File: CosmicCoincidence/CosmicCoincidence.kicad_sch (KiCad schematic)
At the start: 14 parts, among them J1 SJ-43515RS-SMT-TR, J2 SJ-43515RS-SMT-TR, J3 SJ-43515RS-SMT-TR, J4 SJ-43515RS-SMT-TR, J5 SJ-43515RS-SMT-TR, J6 SJ-43515RS-SMT-TR, J7 SJ-43515RS-SMT-TR, J8 SJ-43515RS-SMT-TR, J9 USB_C_Receptacle_USB2.0_14P, SW1 Reset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

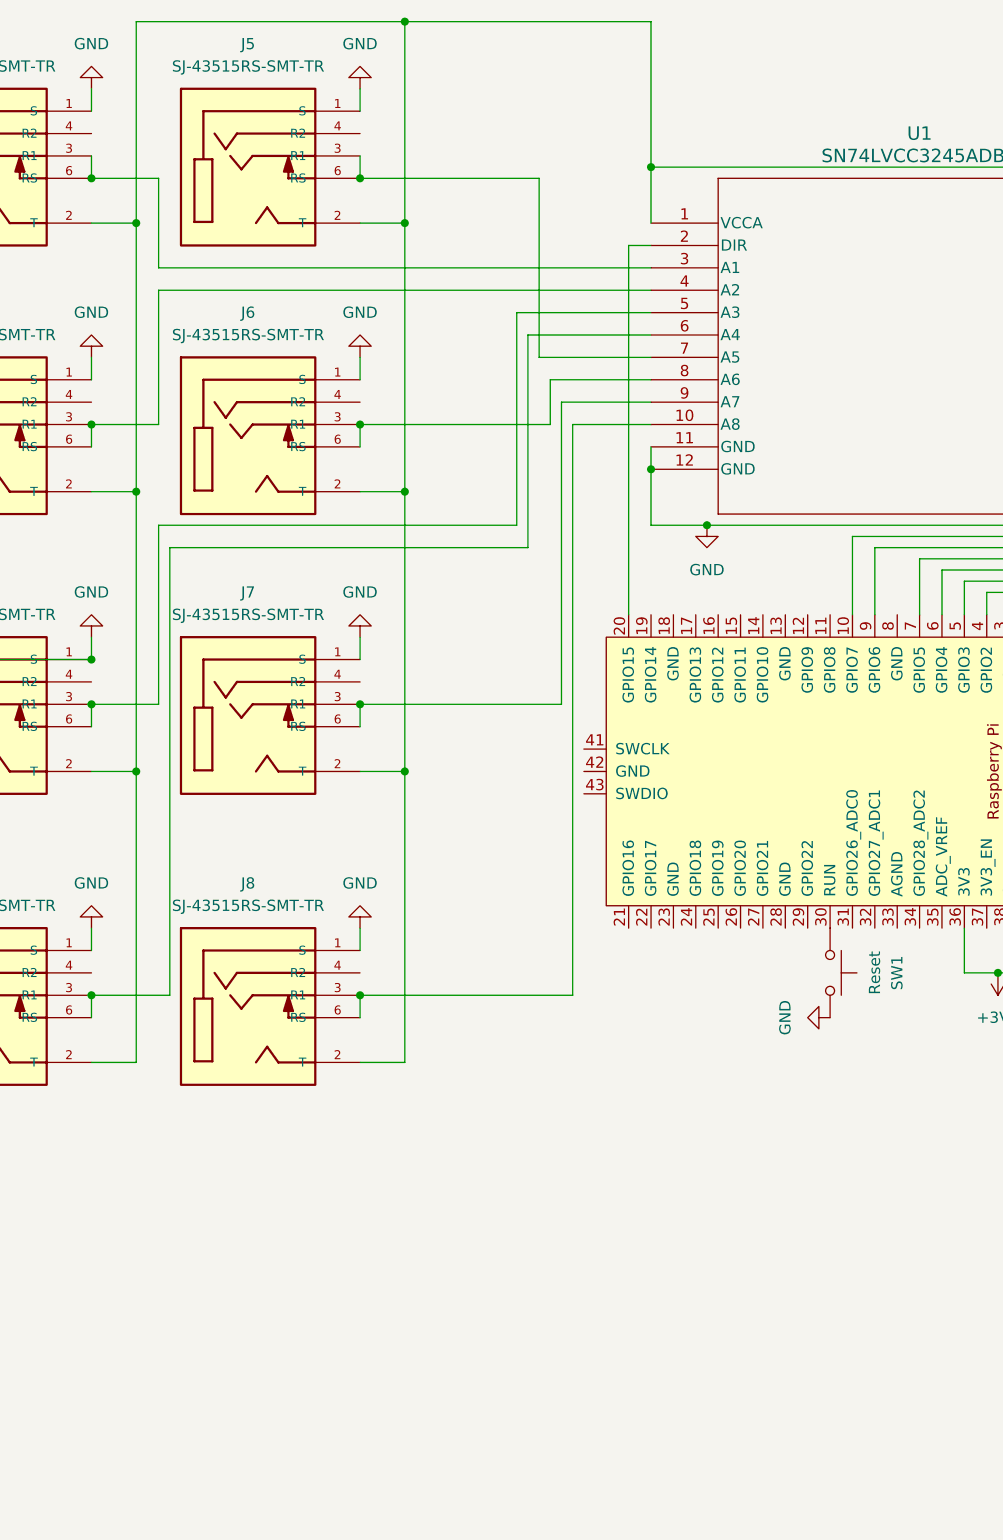
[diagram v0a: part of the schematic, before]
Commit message: Pulldowns on Data Lines
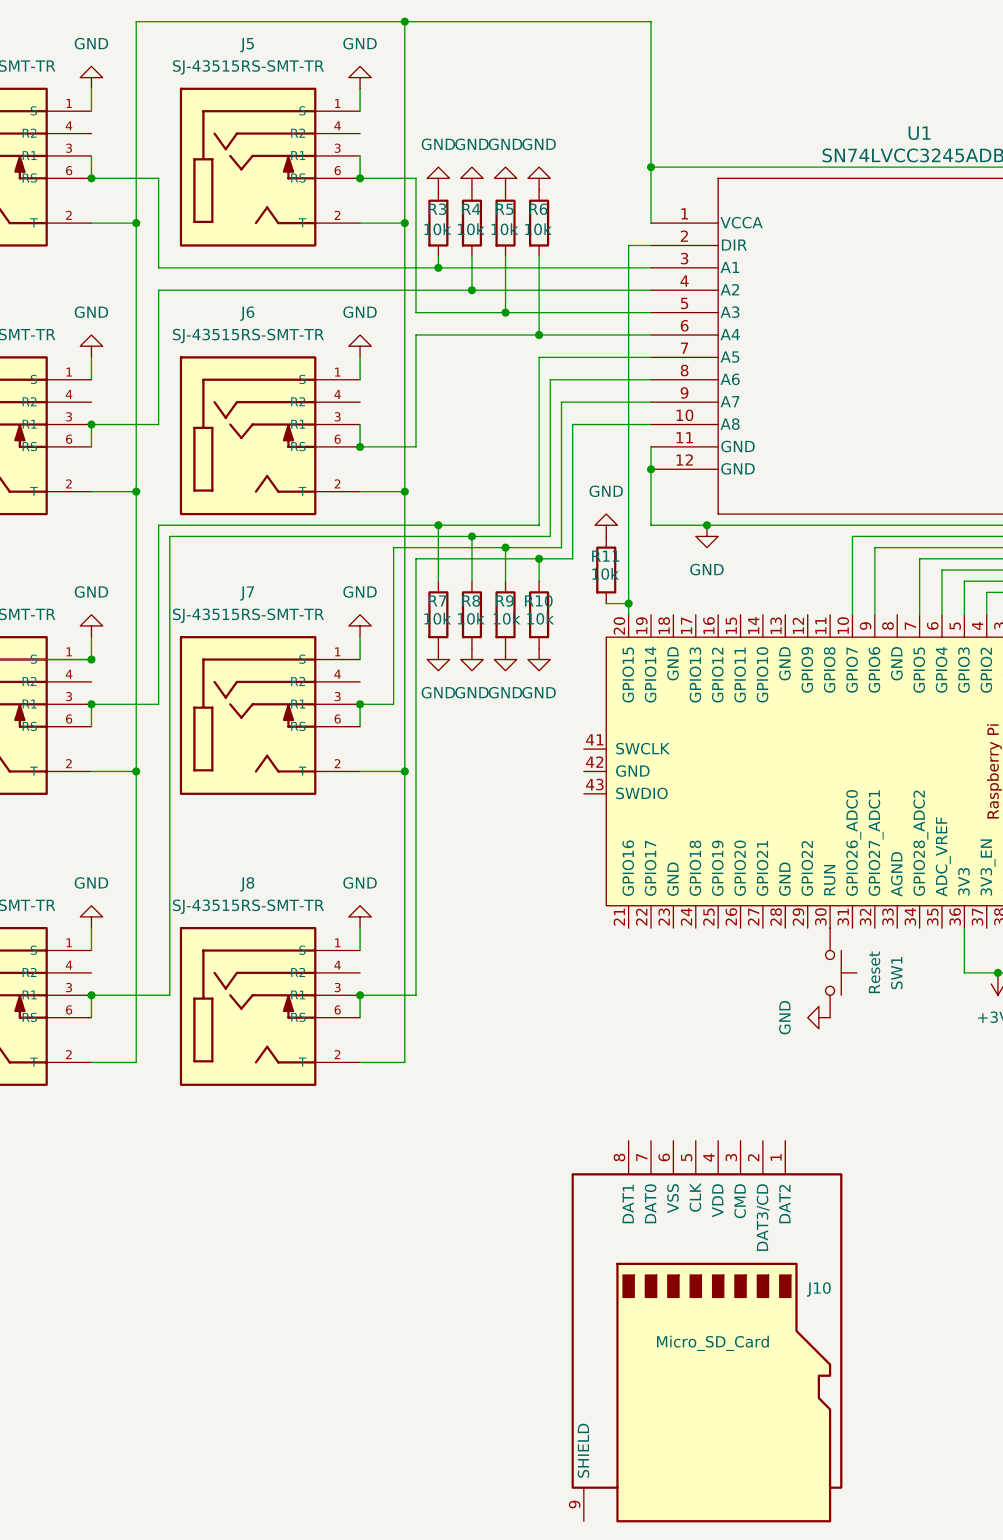
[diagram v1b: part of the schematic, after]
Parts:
- added J10: Micro_SD_Card, symbol Connector:Micro_SD_Card
- added R10, R11, R3, R4, R5, R6, R7, R8, R9: 10k, symbol Device:R
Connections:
- net GND: now also R10.2, R11.1, R3.1, R4.1, R5.1, R6.1, R7.2, R8.2, R9.2
- net at J6.3 (R1), J6.6 (RS): now also U1.6 (A4), R6.2; no longer U1.8 (A6)
- net at J8.3 (R1), J8.6 (RS), U1.10 (A8): now also R10.1
- net at U1.2 (DIR), U2.20 (GPIO15): now also R11.2
- net at J1.3 (R1), J1.6 (RS), U1.3 (A1): now also R3.2
- net at J2.3 (R1), J2.6 (RS), U1.4 (A2): now also R4.2
- net at J3.3 (R1), J3.6 (RS): now also U1.7 (A5), R7.1; no longer U1.5 (A3)
- net at J4.3 (R1), J4.6 (RS): now also U1.8 (A6), R8.1; no longer U1.6 (A4)
- net at J5.3 (R1), J5.6 (RS): now also U1.5 (A3), R5.2; no longer U1.7 (A5)
- net at J7.3 (R1), J7.6 (RS), U1.9 (A7): now also R9.1

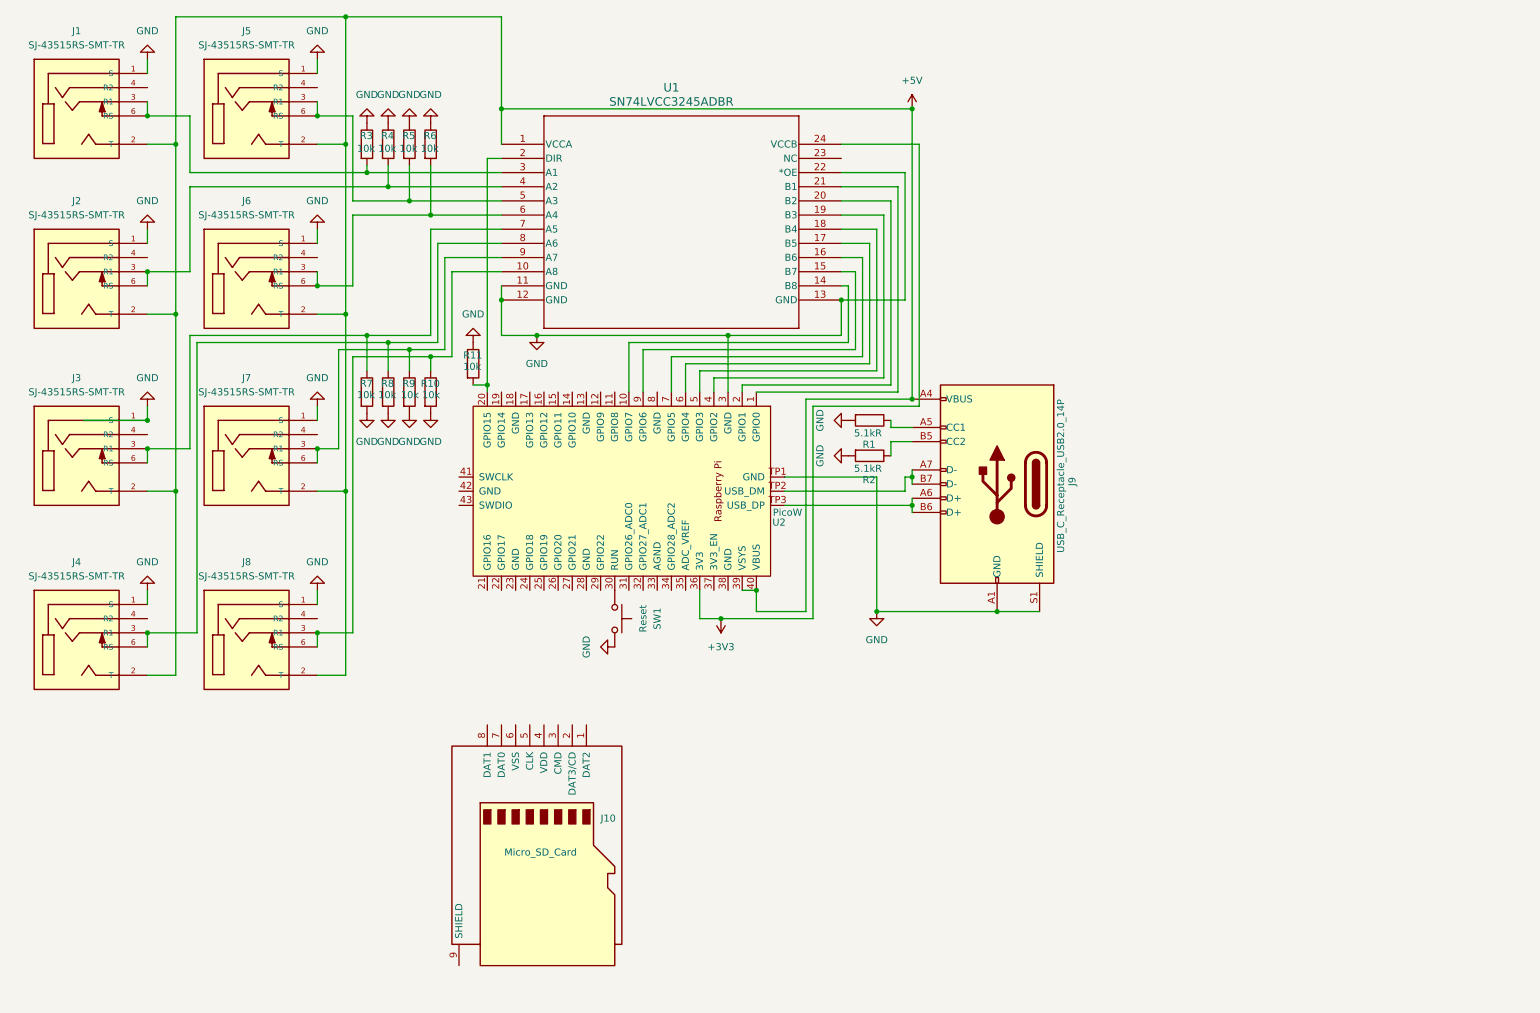
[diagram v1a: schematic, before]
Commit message: Prototype 2
Addition of Power Control, Microsd card, and OLED I2C Screen
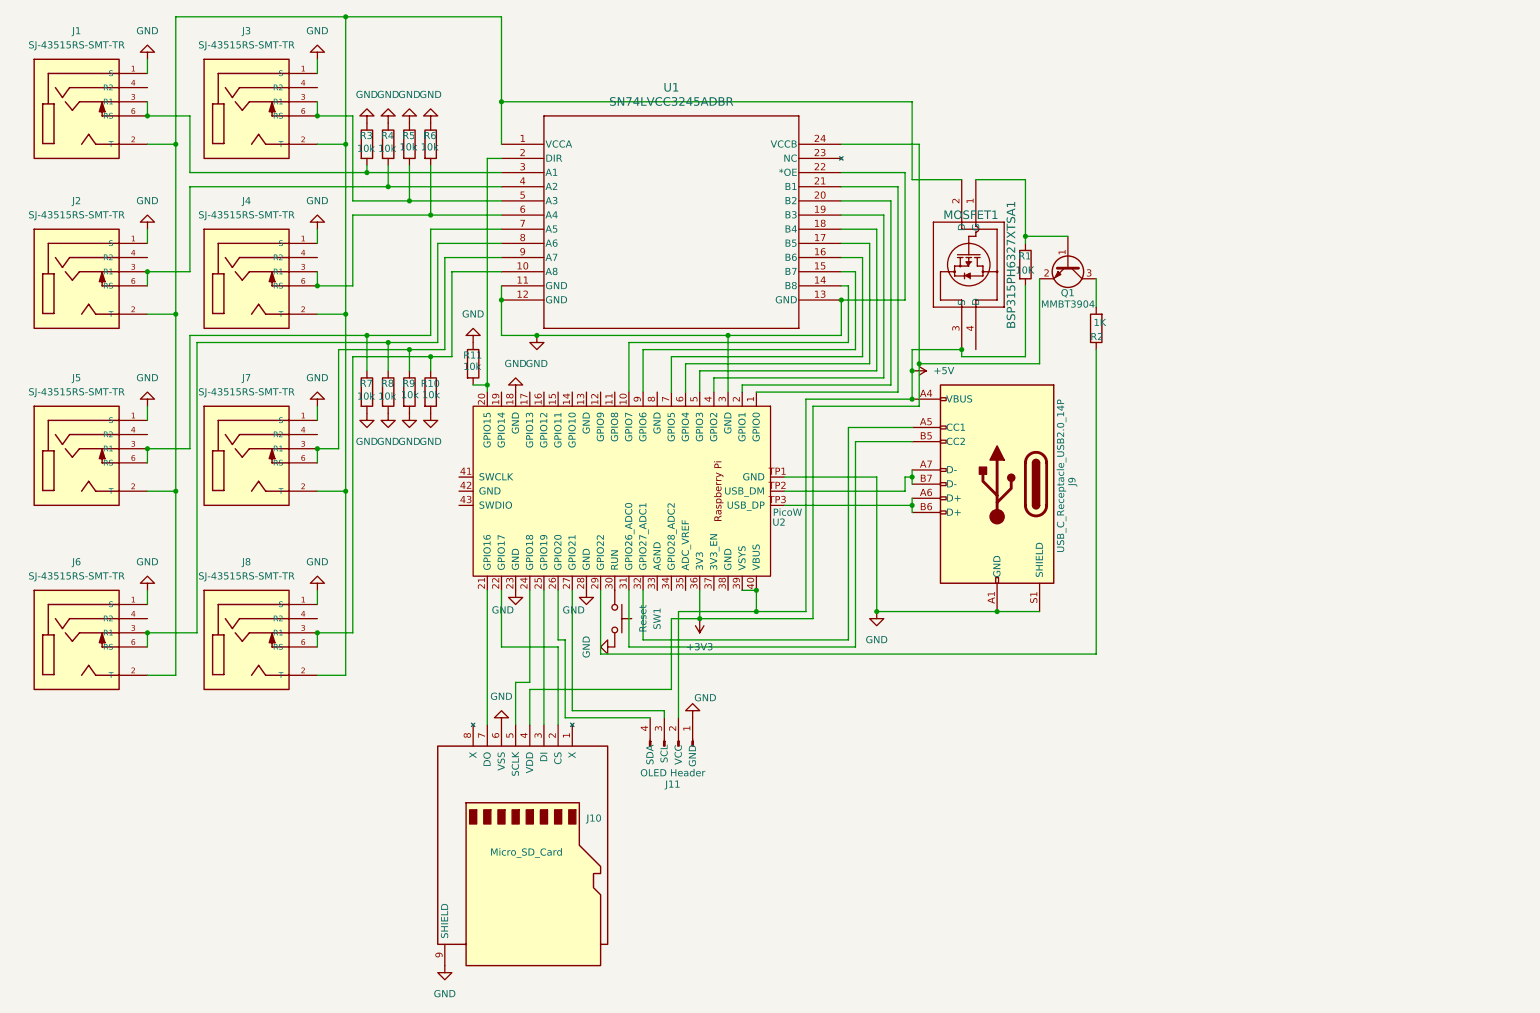
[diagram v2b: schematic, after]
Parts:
- added J11: OLED Header, Connector_PinHeader_2.54mm:PinHeader_1x04_P2.54mm_Vertical, symbol Connector:Conn_01x04_Pin
- added MOSFET1: BSP315PH6327XTSA1, BSP315PH6327XTSA1:PG-SOT223-4_INF, symbol BSP315PH6327XTSA1:BSP315PH6327XTSA1
- added Q1: MMBT3904, Package_TO_SOT_SMD:SOT-23, symbol Transistor_BJT:MMBT3904
- J10: footprint (none) -> Connector_Card:microSD_HC_Molex_47219-2001
- R1: value 5.1kR -> 10K
- R10, R11, R3, R4, R9: footprint (none) -> Resistor_SMD:R_0805_2012Metric
- R2: value 5.1kR -> 1K
- R5: renamed from R7; footprint (none) -> Resistor_SMD:R_0805_2012Metric
- R6: renamed from R8; footprint (none) -> Resistor_SMD:R_0805_2012Metric
- R7: renamed from R5; footprint (none) -> Resistor_SMD:R_0805_2012Metric
- R8: renamed from R6; footprint (none) -> Resistor_SMD:R_0805_2012Metric
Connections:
- net +3V3: now also J10.4 (VDD), Q1.2 (E)
- net +5V: now also R1.2, J11.2 (VCC), MOSFET1.3 (S); no longer J1.2 (T), J2.2 (T), J3.2 (T), J4.2 (T), J5.2 (T), J6.2 (T), J7.2 (T), J8.2 (T), U1.1 (VCCA)
- net GND: now also J10.6 (VSS), J10.9 (SHIELD), R5.1, R6.1, R7.2, R8.2, U2.18 (GND), U2.23 (GND), U2.28 (GND), J11.1 (GND); no longer R1.2, R2.2, R5.2, R6.2, R7.1, R8.1
- net at J6.3 (R1), J6.6 (RS): now also R8.1, U1.8 (A6); no longer R8.2, U1.6 (A4)
- net at J5.3 (R1), J5.6 (RS): now also R7.1, U1.7 (A5); no longer R7.2, U1.5 (A3)
- net at J3.3 (R1), J3.6 (RS): now also R5.2, U1.5 (A3); no longer R5.1, U1.7 (A5)
- net at J4.3 (R1), J4.6 (RS): now also R6.2, U1.6 (A4); no longer R6.1, U1.8 (A6)
- net at J10.2 (CS): now also U2.22 (GPIO17)
- net at J10.3 (DI): now also U2.25 (GPIO19)
- net at J10.5 (SCLK): now also U2.24 (GPIO18)
- net at J10.7 (DO): now also U2.21 (GPIO16)
- net at U2.26 (GPIO20): now also J11.4 (SDA)
- net at U2.27 (GPIO21): now also J11.3 (SCL)
- net at U2.29 (GPIO22): now also R2.1
- net at U2.31 (GPIO26_ADC0): now also J9.B5 (CC2)
- net at U2.32 (GPIO27_ADC1): now also J9.A5 (CC1)
- net at R1.1: now also MOSFET1.1 (G), Q1.1 (B); no longer J9.A5 (CC1)
- new net: J1.2 (T), J2.2 (T), J3.2 (T), J4.2 (T), J5.2 (T), J6.2 (T), J7.2 (T), J8.2 (T), MOSFET1.2 (D), U1.1 (VCCA)
- new net: Q1.3 (C), R2.2
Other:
- moved on the sheet: J3, J4, J5, J6, R5, R6, R7, R8

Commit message: Updated PCB Design (Still no switch footprint)
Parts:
- added R12, R13: 10K, Resistor_SMD:R_0805_2012Metric, symbol Device:R
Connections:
- net +3V3: now also Q1.1 (B); no longer Q1.2 (E)
- net GND: now also R12.2, R13.2
- net at MOSFET1.1 (G), R1.1: now also Q1.3 (C); no longer Q1.1 (B)
- net at R2.2: now also Q1.2 (E); no longer Q1.3 (C)
- net at J9.B5 (CC2), U2.31 (GPIO26_ADC0): now also R12.1
- net at J9.A5 (CC1), U2.32 (GPIO27_ADC1): now also R13.1
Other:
- moved on the sheet: Q1, R2
